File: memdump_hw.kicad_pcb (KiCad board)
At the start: 2 copper layers, 56.1 x 86.1 mm, 76 parts, among them IC1 4094D, IC2 4094D, IC3 4094D, J1 USB_C_USB2.0, J2 SWD, J3 LEVEL, J4 BOOT0, Q1 SI4800, SW1 RESET, U1 AMS1117-3.3, U2 STM32F103C8Tx, U6 SST39SF040, Y1 12M

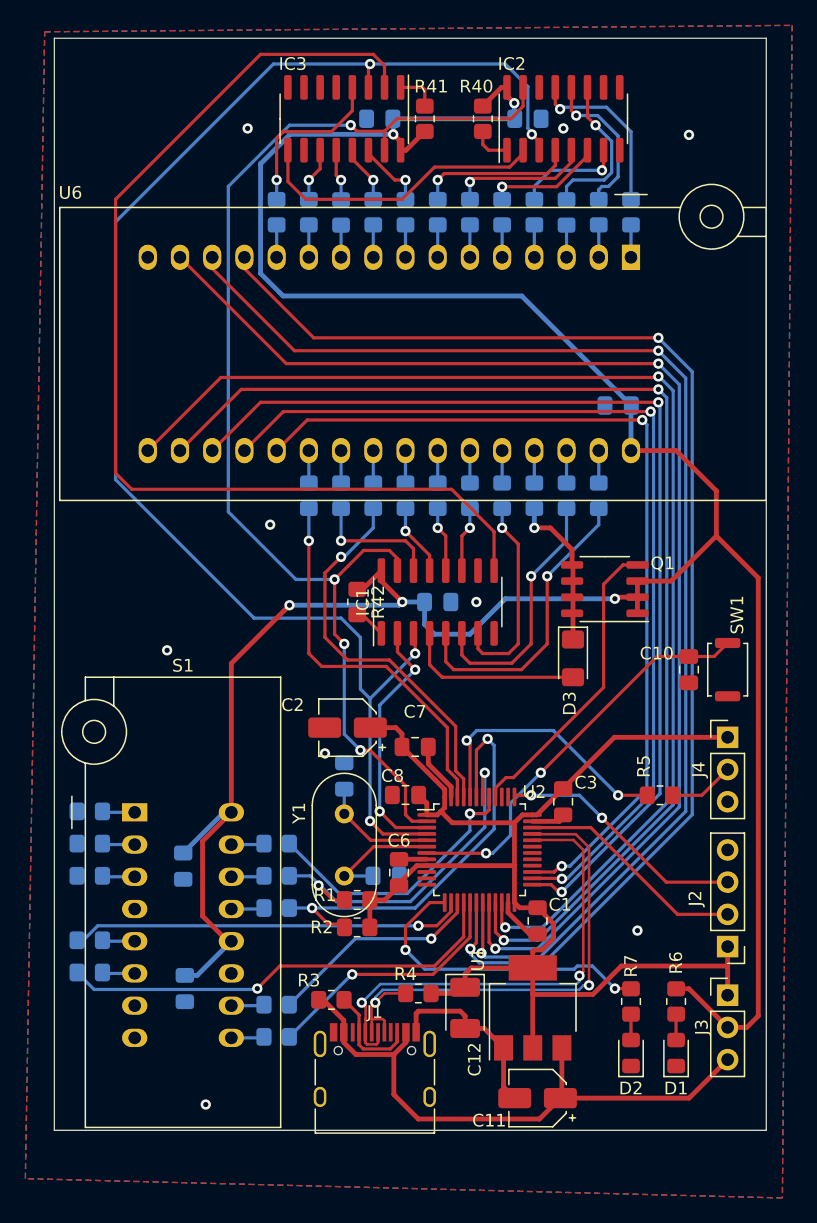
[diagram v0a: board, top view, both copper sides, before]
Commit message: fix: change to 74HC595 fix: all tracks are routed fix: GND is now continuous fix: everything else, the board is pretty much complete
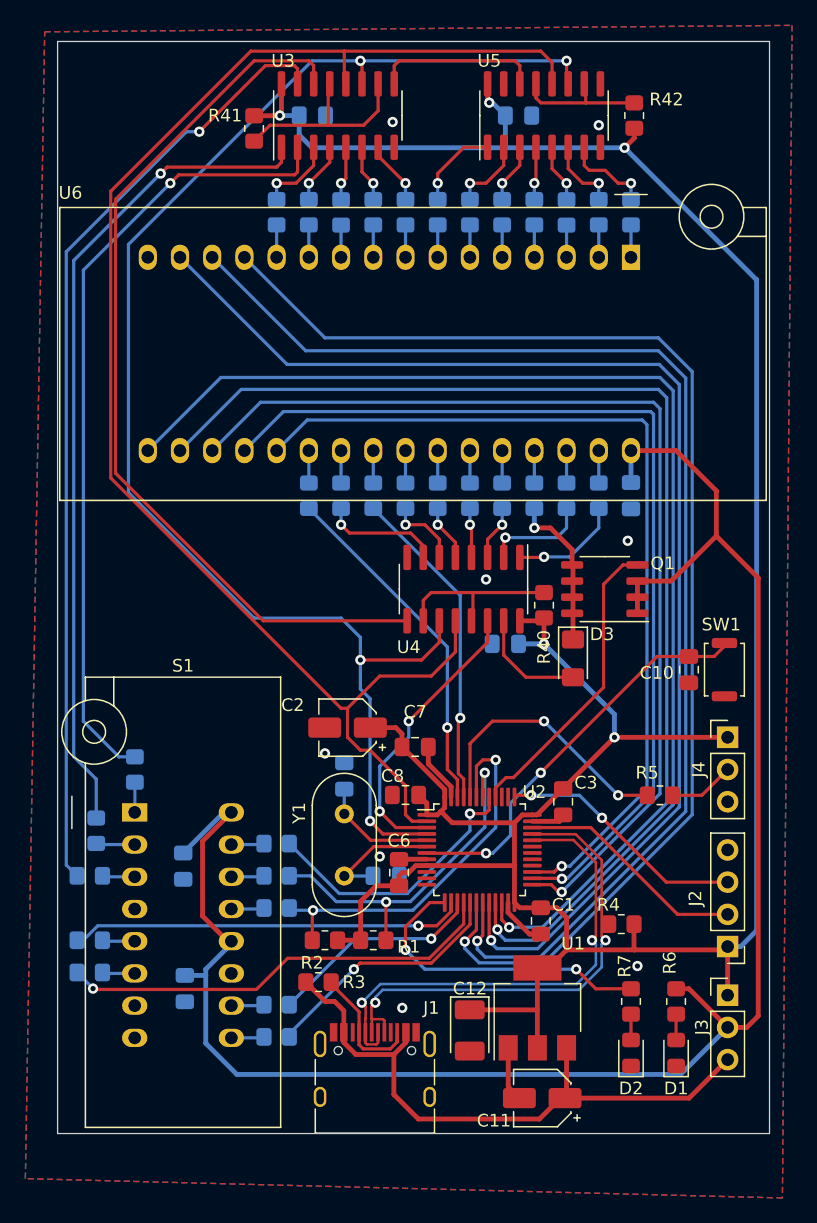
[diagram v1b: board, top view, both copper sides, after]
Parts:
- removed IC1, IC2, IC3: 4094D, Package_SO:SOIC-16_3.9x9.9mm_P1.27mm
- added U3: 74HC595, Package_SO:SOP-16_3.9x9.9mm_P1.27mm, F.Cu at (190.8, 62.5)
- added U4: 74HC595, Package_SO:SOP-16_3.9x9.9mm_P1.27mm, F.Cu at (200.7, 99.8)
- added U5: 74HC595, Package_SO:SOP-16_3.9x9.9mm_P1.27mm, F.Cu at (207.0, 62.5)
- U2: value STM32F103C8Tx -> STM32F103C8
- moved R42 44.1 mm to (214.1, 62.5), turned to 90 degrees
- moved C13 41.4 mm to (204.0, 104.1), turned to 180 degrees
- moved C15 38.9 mm to (205.0, 62.5)
- moved R40 38.7 mm to (207.0, 101.1), turned to 90 degrees
- moved R4 16.9 mm to (213.1, 126.2)
- moved R41 13.5 mm to (184.2, 63.5), turned to -90 degrees
- moved C18 7.18 mm to (213.9, 92.5), turned to -90 degrees
- moved C14 5.32 mm to (188.7, 62.5), turned to 0 degrees
- moved R30 4.85 mm to (174.8, 114.0), turned to -90 degrees
- moved R1 3.42 mm to (193.5, 127.5), turned to 180 degrees
- moved R2 2.74 mm to (189.7, 127.5)
- moved C12 1.82 mm to (201.2, 134.6)
- moved R3 1.73 mm to (189.2, 130.8)
- moved R31 1.14 mm to (171.7, 118.9), turned to -90 degrees
- moved C11 0.37 mm to (206.9, 140.0)
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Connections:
- C13 pad 1: VBUS -> +3.3VA
- C14 pad 1: VBUS -> +3.3VA
- C15 pad 1: VBUS -> +3.3VA
- R40 pad 1: VBUS -> +3.3VA
- R41 pad 1: VBUS -> +3.3VA
- R42 pad 1: VBUS -> +3.3VA
- U2 pad 2: AE -> AST
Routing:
- net +3.3VA: track 103.4 -> 228.7 mm, vias 0 -> 5
- net AST: track 0.00 -> 118.1 mm
- net AE: track 96.0 -> 0.00 mm, vias 4 -> 0
- net VBUS: track 221.4 -> 142.2 mm, vias 5 -> 0
- net I2C_A2: track 0.00 -> 75.2 mm, vias 0 -> 1
- net I2C_A1: track 0.00 -> 65.5 mm, vias 0 -> 1
- net I2C_A0: track 0.00 -> 62.8 mm, vias 0 -> 1
- net A19: track 23.7 -> 8.73 mm
- net SO1: track 84.4 -> 71.1 mm
- net Net-(R41-Pad2): track 3.27 -> 16.0 mm
- net A13+NWE: track 16.1 -> 4.34 mm
- net A17: track 19.9 -> 8.30 mm
- net GND: track 28.0 -> 17.5 mm
- net Net-(R40-Pad2): track 3.12 -> 13.5 mm
- net SO2: track 23.4 -> 13.1 mm
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
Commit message: fix: pcb implementation of schematic changes fix: less sharp corners feat: more ground infill with GND vias
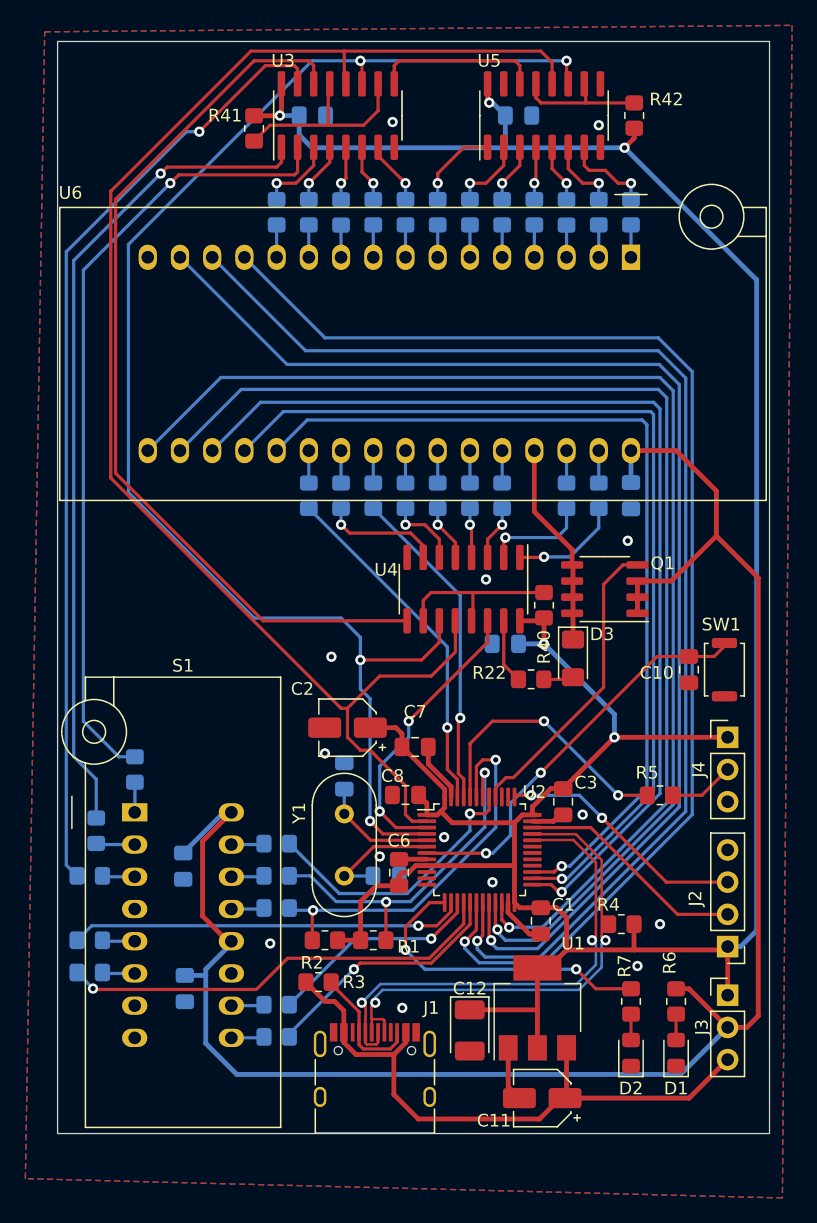
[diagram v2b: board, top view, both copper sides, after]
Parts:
- R10, R11, R12, R13, R14, R15, R16, R17, R18, R19, R20, R21, R23, R24, R25, R26, R27, R28, R29, R30, R31, R32, R33, R34, R35, R36, R37, R38, R39, R8, R9: value 10k -> 470
- R22: value 10k -> 470; moved to F.Cu
- moved R22 14.5 mm to (206.0, 106.9), turned to 0 degrees
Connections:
- D3 pad 2: A14 -> Net-(D3-Pad2)
- R22 pad 1: A14+VCC_28 -> A14
- R22 pad 2: Net-(R22-Pad2) -> Net-(D3-Pad2)
- U6 pad 29: Net-(R22-Pad2) -> A14+VCC_28
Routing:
- net A14+VCC_28: track 12.2 -> 16.1 mm, vias 1 -> 0
- net A14: track 8.89 -> 5.09 mm
- net Net-(R22-Pad2): track 2.56 -> 0.00 mm
- net Net-(D3-Pad2): track 0.00 -> 2.37 mm
- net +3.3VA: track 228.7 -> 229.5 mm
- net GND: track 17.5 -> 17.6 mm, vias 8 -> 14
